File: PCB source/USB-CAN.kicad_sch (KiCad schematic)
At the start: 19 parts, among them U9 STM32G431C8Tx

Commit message: Do Cleanup
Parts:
- removed C42, C43, C44, C45: 100n, Capacitor_SMD:C_0402_1005Metric, symbol Device:C
- removed C46: 1u, Capacitor_SMD:C_0603_1608Metric, symbol Device:C
- removed C47: 4.7u, Capacitor_SMD:C_0603_1608Metric, symbol Device:C
- removed C48: 10u, Capacitor_SMD:C_0805_2012Metric, symbol Device:C
- removed D2: WORD_LED, Diode_SMD:D_0603_1608Metric, symbol Device:LED
- removed D3: STAT_LED, Diode_SMD:D_0603_1608Metric, symbol Device:LED
- added C18, C19, C20, C21, C22, C23: 100nF, PCM_JLCPCB:C_0402, symbol PCM_JLCPCB-Capacitors:0402,100nF
- added C24: 10uF, PCM_JLCPCB:C_0402, symbol PCM_JLCPCB-Capacitors:0402,10uF
- added D2, D3: Green, PCM_JLCPCB:D_0603, symbol PCM_JLCPCB-Diodes:LED,0603,Green
- TP1, TP2, TP3, TP4, TP5: footprint TestPoint:TestPoint_Pad_1.0x1.0mm -> TestPoint:TestPoint_Pad_D1.0mm
- renumbered C49 to C25, R20 to R10, R21 to R11, R19 to R9, U9 to U3
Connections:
- net +3V3: now also C18.1, C19.1, C20.1, C21.1, C22.1, C23.1, C24.1, D2.2, D3.2
- net GND: now also C18.2, C19.2, C20.2, C21.2, C22.2, C23.2, C24.2
- net STAT_LED1: no longer U3.39 (PA15)
- net WORD_LED1: no longer U3.8 (PA0)
- net at R11.2: now also D3.1
- net at R10.2: now also D2.1
- net LED_RX: now reaches U3.9 (PA1)
- new net LED_TX: U3.8 (PA0)
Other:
- moved on the sheet: C25, R9, TP1, TP2, TP3, TP4, TP5, U3

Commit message: Pass ERC
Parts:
- added C17, C59: 100nF, PCM_JLCPCB:C_0402, symbol PCM_JLCPCB-Capacitors:0402,100nF
- added U13: AMS1117-3.3, Package_TO_SOT_SMD:SOT-223-3_TabPin2, symbol Regulator_Linear:AMS1117-3.3
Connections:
- net STAT_LED1 is gone; now on net LED_TX: R11.1
- net WORD_LED1 is gone; now on net LED_RX: R10.1
- net +3V3: now also C17.1, U13.2 (VO)
- net GND: now also C17.2, C59.2, U13.1 (GND)
- new net +5V: C59.1, U13.3 (VI)
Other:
- moved on the sheet: D2, D3, R10, R11

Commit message: Prepare board for layout
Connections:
- net USB_CAN.+ renamed USB_CAN.D+
- net USB_CAN.- renamed USB_CAN.D-
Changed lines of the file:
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@@
 		)
 	)
-	(label "USB_CAN.-"
+	(label "USB_CAN.D-"
 		(at 196.85 93.98 180)
 		(fields_autoplaced yes)
@@
 		)
 	)
-	(label "USB_CAN.+"
+	(label "USB_CAN.D+"
 		(at 196.85 96.52 180)
 		(fields_autoplaced yes)

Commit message: Do buck Layout
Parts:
- removed D2: Green, PCM_JLCPCB:D_0603, symbol PCM_JLCPCB-Diodes:LED,0603,Green
- added D1: Yellow, PCM_JLCPCB:D_0603, symbol PCM_JLCPCB-Diodes:LED,0603,Yellow
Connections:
- net +3V3: now also D1.2
- net at R10.2: now also D1.1
- net STAT_LED: now reaches U3.39 (PA15)
- net STAT_LED: now also R10.1
- net LED_RX: no longer names the net of U3.9 (PA1)
- net LED_RX: no longer R10.1
- net LED_TX renamed WORD_LED

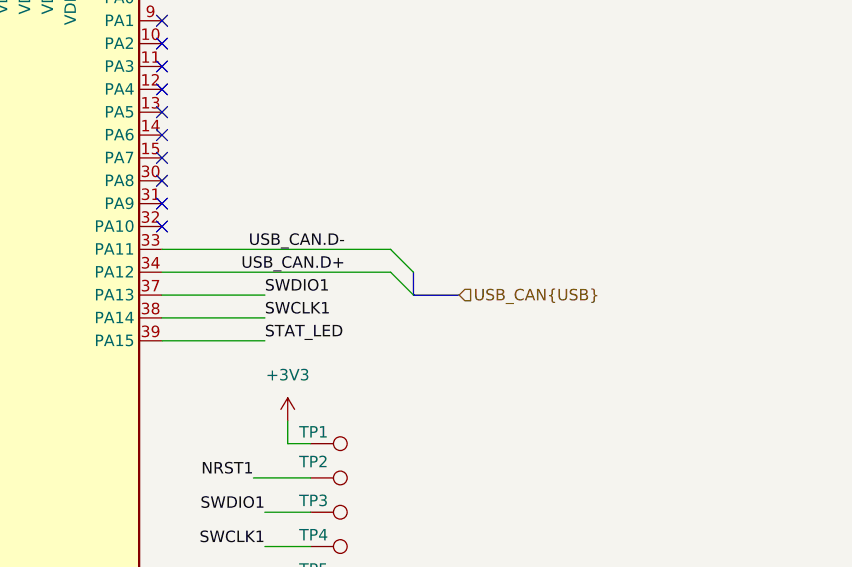
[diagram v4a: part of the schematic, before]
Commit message: Add 22R resistors to USB
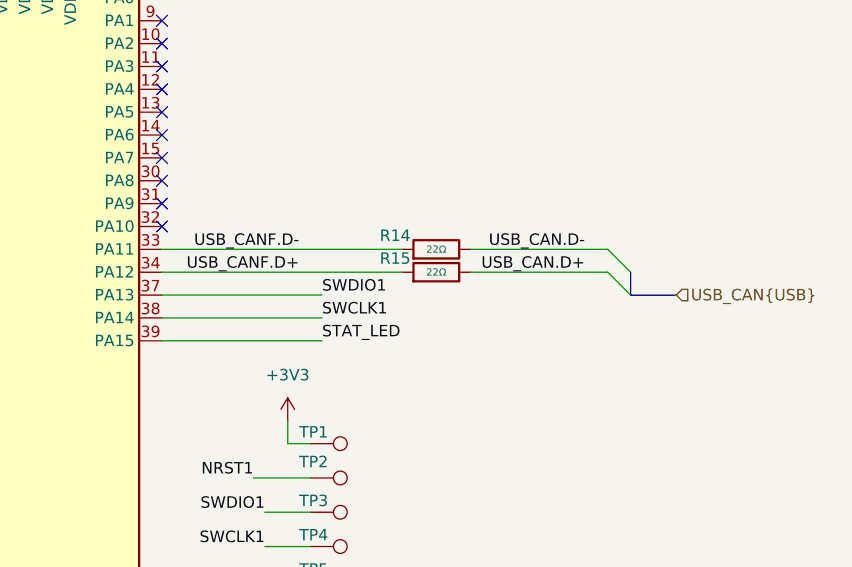
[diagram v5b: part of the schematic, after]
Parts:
- added R14, R15: 22Ω, PCM_JLCPCB:R_0402, symbol PCM_JLCPCB-Resistors:0402,22Ω
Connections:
- net USB_CAN.D+: now also R15.2; no longer U3.34 (PA12)
- net USB_CAN.D-: now also R14.2; no longer U3.33 (PA11)
- new net USB_CANF.D+: R15.1, U3.34 (PA12)
- new net USB_CANF.D-: R14.1, U3.33 (PA11)

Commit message: Fix schematic
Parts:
- C17, C18, C19, C20, C21, C22, C23, C59: Stock 27771805 -> 19831671
- C24: Price 0.007USD -> 0.008USD; Stock 9197991 -> 1226257
- R14, R15: Stock 2497993 -> 2158519
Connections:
- net NRST1 renamed NRST
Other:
- moved on the sheet: U3

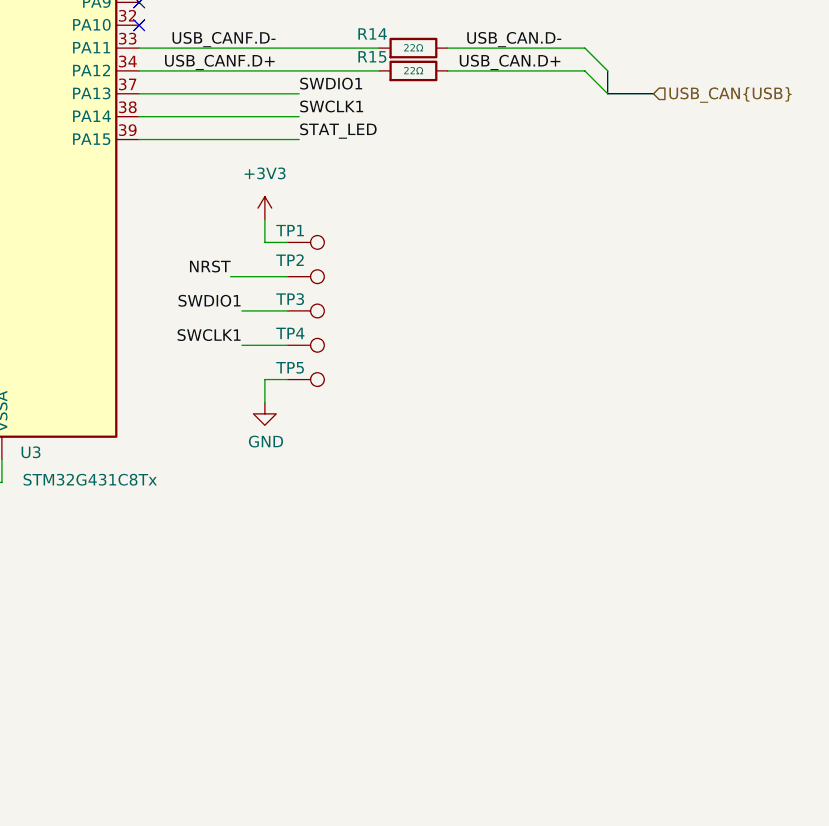
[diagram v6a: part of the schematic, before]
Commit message: Fix can power delivery , fixed placment of the mosfets, CAN power  pull down to avoid DFU boot, added new porgraming connector
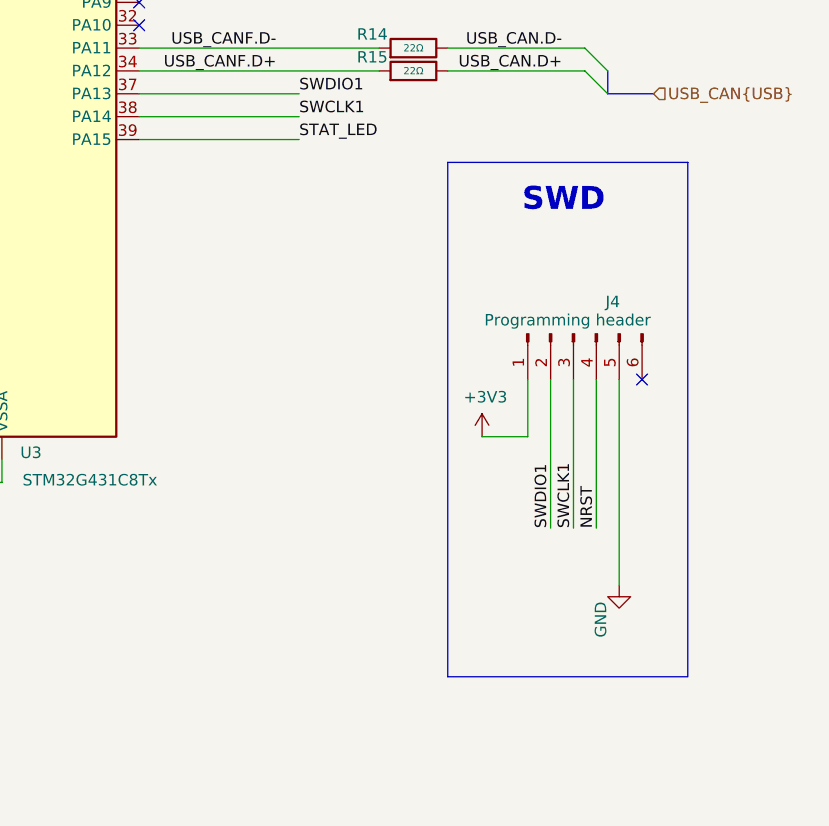
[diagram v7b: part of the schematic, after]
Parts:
- removed TP1, TP2, TP3, TP4, TP5: ~, TestPoint:TestPoint_Pad_D1.0mm, symbol Connector:TestPoint
- added J4: Programming header, Connector_PinHeader_1.27mm:PinHeader_1x06_P1.27mm_Vertical, symbol Connector:Conn_01x06_Pin
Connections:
- net +3V3: now also J4.1 (Pin_1)
- net GND: now also J4.5 (Pin_5)
- net NRST: now also J4.4 (Pin_4)
- net SWCLK1: now also J4.3 (Pin_3)
- net SWDIO1: now also J4.2 (Pin_2)
- no-connect marks 29 -> 30
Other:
- note added: "SWD"
